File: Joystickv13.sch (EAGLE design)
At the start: 56 parts, among them J1 AVR_SPI_PRG_6PTH, U1 JOYSTICKPTH, U3 V_REG_MIC5219SMD, U4 MCP73831

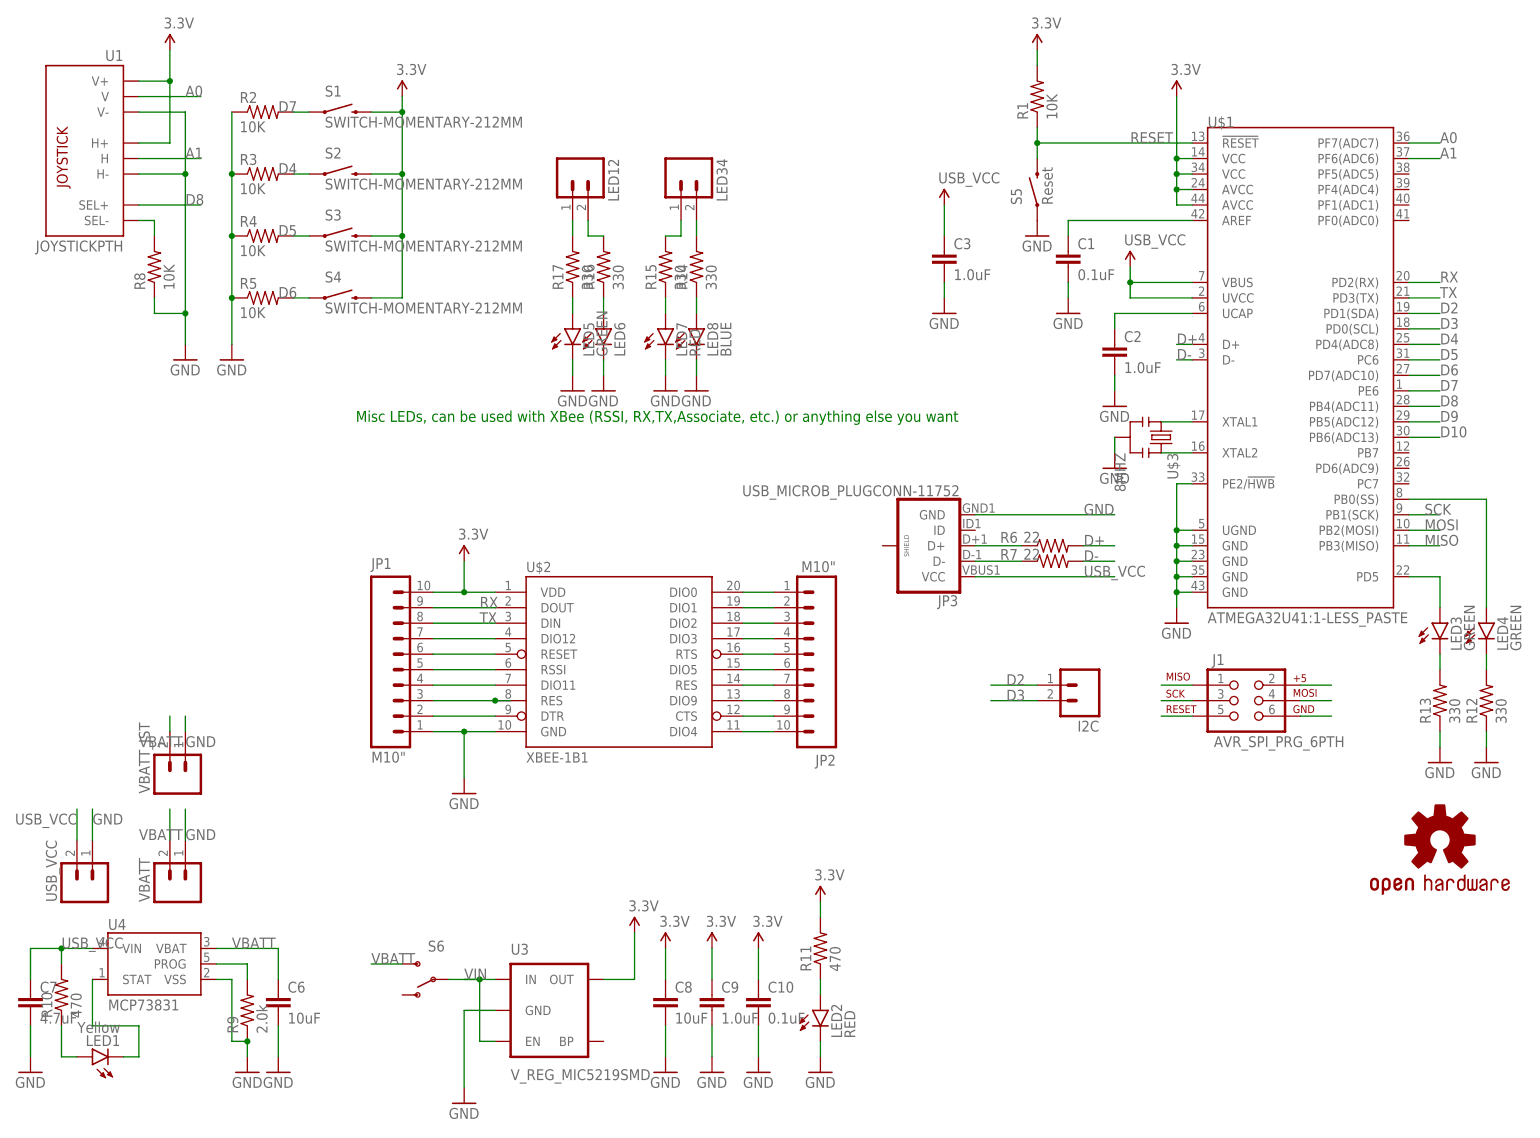
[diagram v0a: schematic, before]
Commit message: Panel
Finished design, Panelized, and CAMed
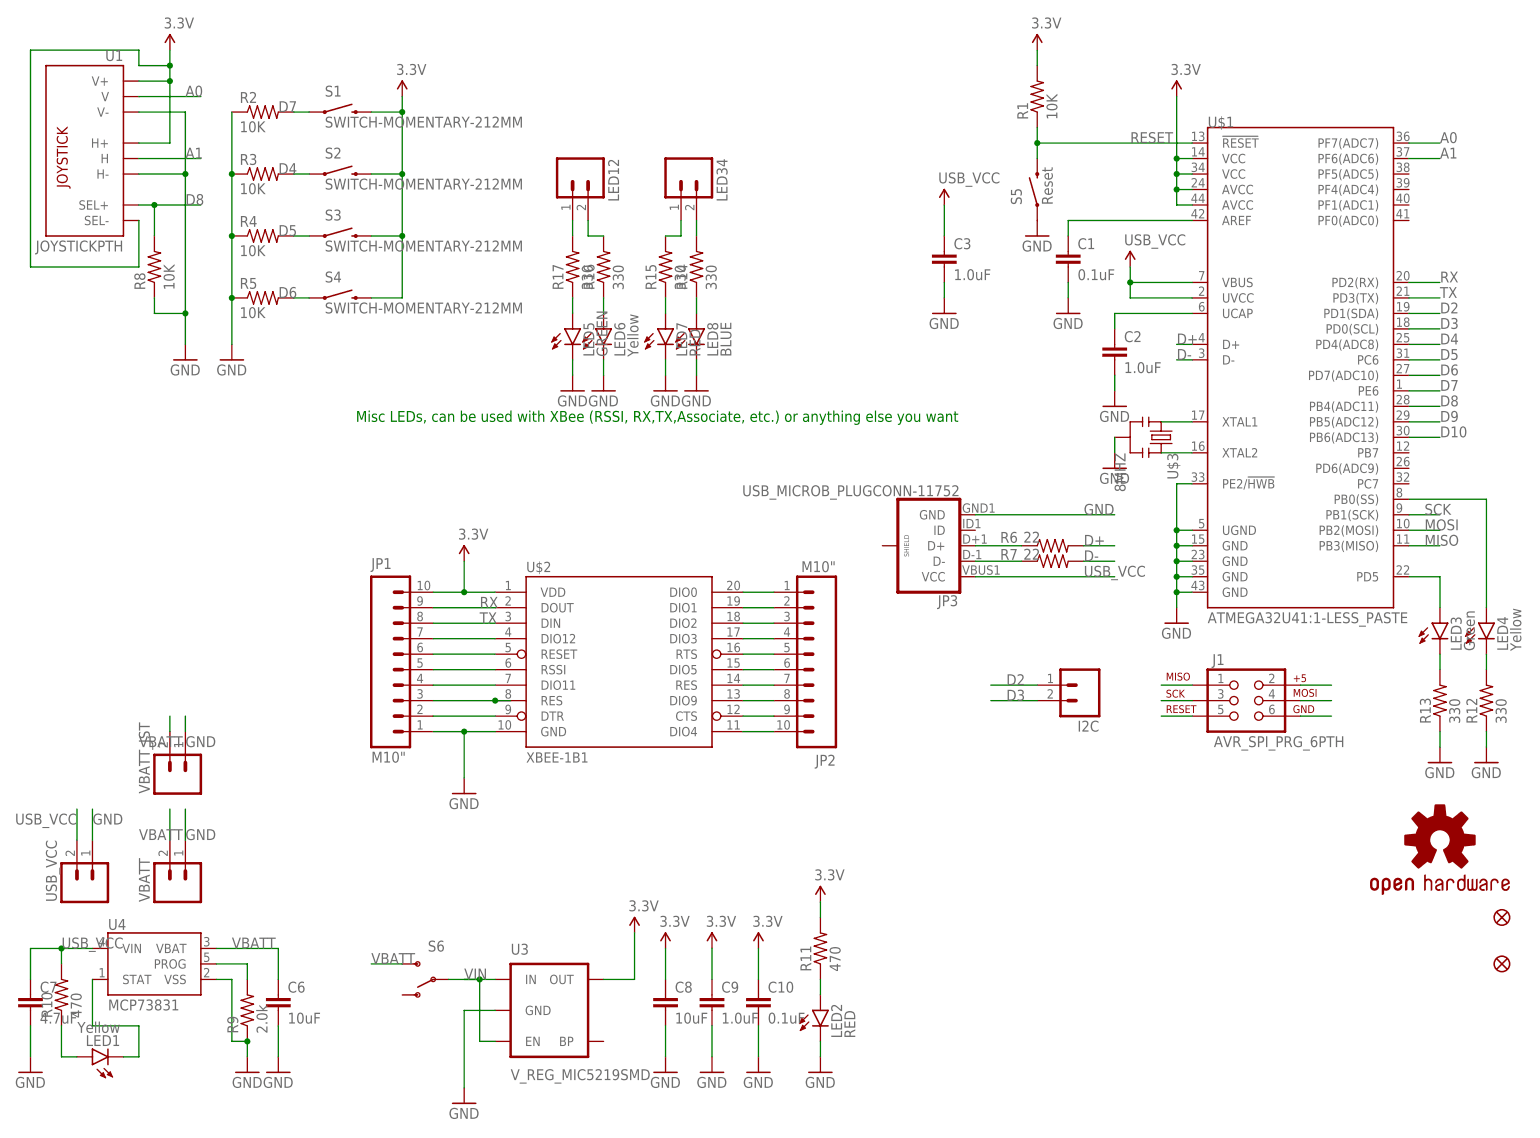
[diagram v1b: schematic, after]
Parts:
- added FID1, FID2: FIDUCIALUFIDUCIAL, SparkFun-Aesthetics:FIDUCIALUFIDUCIAL
- LED3: value GREEN -> Green
- LED4: value GREEN -> Yellow
- LED6: value (none) -> Yellow
- LOGO1: value OSHW-LOGOL -> OSHW-LOGOM; device SparkFun-Aesthetics:OSHW-LOGOL -> SparkFun-Aesthetics:OSHW-LOGOM
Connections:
- removed net N$22: R8.2, U1.SEL-
- net 3.3V: now also U1.SEL-
- net D8: now also R8.2
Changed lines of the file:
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@@
 <layer number="56" name="wert" color="7" fill="1" visible="no" active="no"/>
 <layer number="57" name="tCAD" color="7" fill="1" visible="no" active="no"/>
+<layer number="59" name="tCarbon" color="7" fill="1" visible="no" active="no"/>
+<layer number="60" name="bCarbon" color="7" fill="1" visible="no" active="no"/>
 <layer number="90" name="Modules" color="5" fill="1" visible="yes" active="yes"/>
 <layer number="91" name="Nets" color="2" fill="1" visible="yes" active="yes"/>
@@
 <layer number="127" name="_tValues" color="7" fill="1" visible="yes" active="yes"/>
 <layer number="128" name="_bValues" color="7" fill="1" visible="yes" active="yes"/>
+<layer number="129" name="Mask" color="7" fill="1" visible="yes" active="yes"/>
 <layer number="131" name="tAdjust" color="7" fill="1" visible="yes" active="yes"/>
 <layer number="132" name="bAdjust" color="7" fill="1" visible="yes" active="yes"/>
@@
 <layer number="223" name="223bmp" color="24" fill="1" visible="no" active="no"/>
 <layer number="224" name="224bmp" color="25" fill="1" visible="no" active="no"/>
+<layer number="225" name="225bmp" color="7" fill="1" visible="yes" active="yes"/>
+<layer number="226" name="226bmp" color="7" fill="1" visible="yes" active="yes"/>
+<layer number="227" name="227bmp" color="7" fill="1" visible="yes" active="yes"/>
+<layer number="228" name="228bmp" color="7" fill="1" visible="yes" active="yes"/>
+<layer number="229" name="229bmp" color="7" fill="1" visible="yes" active="yes"/>
+<layer number="230" name="230bmp" color="7" fill="1" visible="yes" active="yes"/>
+<layer number="231" name="231bmp" color="7" fill="1" visible="yes" active="yes"/>
 <layer number="248" name="Housing" color="7" fill="1" visible="yes" active="yes"/>
 <layer number="249" name="Edge" color="7" fill="1" visible="yes" active="yes"/>
@@
 <part name="LED1" library="SparkFun-LED" deviceset="LED-YELLOW" device="0603" value="Yellow"/>
 <part name="LED2" library="SparkFun-LED" deviceset="LED-RED" device="0603" value="RED"/>
-<part name="LED3" library="SparkFun-LED" deviceset="LED-GREEN" device="0603" value="GREEN"/>
-<part name="LED4" library="SparkFun-LED" deviceset="LED-YELLOW" device="0603" value="GREEN"/>
+<part name="LED3" library="SparkFun-LED" deviceset="LED-GREEN" device="0603" value="Green"/>
+<part name="LED4" library="SparkFun-LED" deviceset="LED-YELLOW" device="0603" value="Yellow"/>
 <part name="LED5" library="SparkFun-LED" deviceset="LED-GREEN" device="0603" value="GREEN"/>
-<part name="LED6" library="SparkFun-LED" deviceset="LED-YELLOW" device="0603"/>
+<part name="LED6" library="SparkFun-LED" deviceset="LED-YELLOW" device="0603" value="Yellow"/>
 <part name="LED7" library="SparkFun-LED" deviceset="LED-RED" device="0603" value="RED"/>
 <part name="LED8" library="SparkFun-LED" deviceset="LED-BLUE" device="0603" value="BLUE"/>
@@
 <part name="S3" library="SparkFun-Electromechanical" deviceset="SWITCH-MOMENTARY-2" device="12MM"/>
 <part name="S4" library="SparkFun-Electromechanical" deviceset="SWITCH-MOMENTARY-2" device="12MM"/>
-<part name="LOGO1" library="SparkFun-Aesthetics" deviceset="OSHW-LOGO" device="L"/>
+<part name="LOGO1" library="SparkFun-Aesthetics" deviceset="OSHW-LOGO" device="M" value="OSHW-LOGOM"/>
+<part name="FID1" library="SparkFun-Aesthetics" deviceset="FIDUCIAL" device="UFIDUCIAL"/>
+<part name="FID2" library="SparkFun-Aesthetics" deviceset="FIDUCIAL" device="UFIDUCIAL"/>
 </parts>
 <sheets>
@@
 <instance part="S4" gate="G$1" x="0" y="119.38"/>
 <instance part="LOGO1" gate="G$1" x="180.34" y="30.48"/>
+<instance part="FID1" gate="G$1" x="190.5" y="17.78"/>
+<instance part="FID2" gate="G$1" x="190.5" y="10.16"/>
 </instances>
 <busses>
@@
 <junction x="-27.94" y="154.94"/>
 <pinref part="P+1" gate="G$1" pin="3.3V"/>
-<wire x1="-27.94" y1="154.94" x2="-27.94" y2="160.02" width="0.1524" layer="91"/>
+<wire x1="-27.94" y1="154.94" x2="-27.94" y2="157.48" width="0.1524" layer="91"/>
+<pinref part="U1" gate="G$1" pin="SEL-"/>
+<wire x1="-27.94" y1="157.48" x2="-27.94" y2="160.02" width="0.1524" layer="91"/>
+<wire x1="-33.02" y1="132.08" x2="-33.02" y2="124.46" width="0.1524" layer="91"/>
+<wire x1="-33.02" y1="124.46" x2="-50.8" y2="124.46" width="0.1524" layer="91"/>
+<wire x1="-50.8" y1="124.46" x2="-50.8" y2="160.02" width="0.1524" layer="91"/>
+<wire x1="-50.8" y1="160.02" x2="-33.02" y2="160.02" width="0.1524" layer="91"/>
+<wire x1="-33.02" y1="160.02" x2="-33.02" y2="157.48" width="0.1524" layer="91"/>
+<wire x1="-33.02" y1="157.48" x2="-27.94" y2="157.48" width="0.1524" layer="91"/>
+<junction x="-27.94" y="157.48"/>
 </segment>
 <segment>
@@
 </segment>
 </net>
-<net name="N$22" class="0">
-<segment>
-<pinref part="R8" gate="G$1" pin="2"/>
-<wire x1="-30.48" y1="129.54" x2="-30.48" y2="132.08" width="0.1524" layer="91"/>
-<pinref part="U1" gate="G$1" pin="SEL-"/>
-<wire x1="-30.48" y1="132.08" x2="-33.02" y2="132.08" width="0.1524" layer="91"/>
-</segment>
-</net>
 <net name="D2" class="0">
 <segment>
@@
 <segment>
 <pinref part="U1" gate="G$1" pin="SEL+"/>
-<wire x1="-33.02" y1="134.62" x2="-22.86" y2="134.62" width="0.1524" layer="91"/>
+<wire x1="-33.02" y1="134.62" x2="-30.48" y2="134.62" width="0.1524" layer="91"/>
 <label x="-25.4" y="134.62" size="1.778" layer="95"/>
-</segment>
-<segment>
+<pinref part="R8" gate="G$1" pin="2"/>
+<wire x1="-30.48" y1="134.62" x2="-22.86" y2="134.62" width="0.1524" layer="91"/>
+<wire x1="-30.48" y1="134.62" x2="-30.48" y2="129.54" width="0.1524" layer="91"/>
+<junction x="-30.48" y="134.62"/>
+</segment>
+<segment>
